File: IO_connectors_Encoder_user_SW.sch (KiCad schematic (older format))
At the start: 36 parts, among them IC1 TPD4E001DRLR, IC2 74AUP1G74DC.125, IC3 CD74HC4050PWR, SW1 TL1100CF160Q, SW2 PEC16-2215F-S0024, X1 DS1024-2*20R0, X2 DS1013-16SSIB1, X3 691322110005

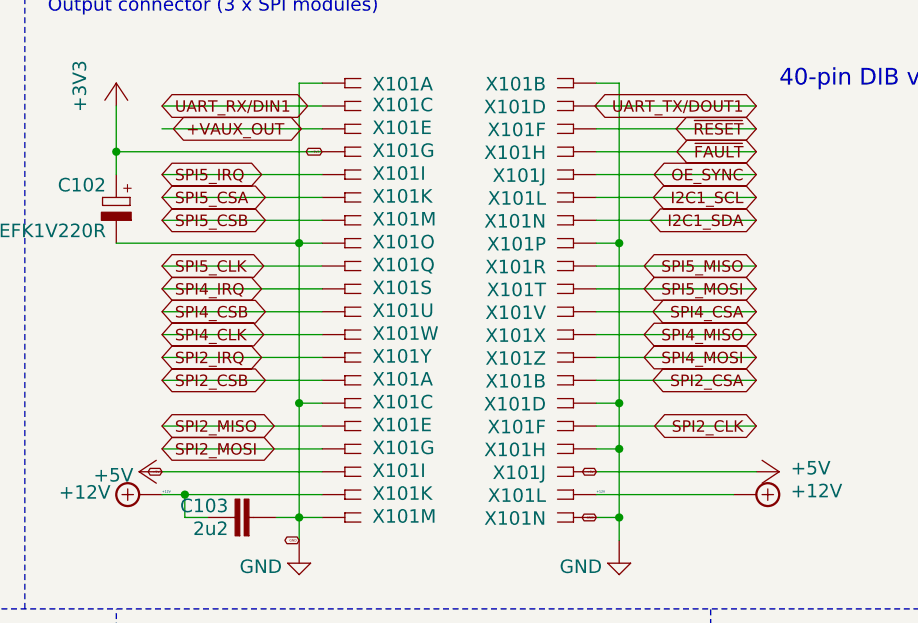
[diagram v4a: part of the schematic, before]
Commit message: Adding TO FROM FPGA lines
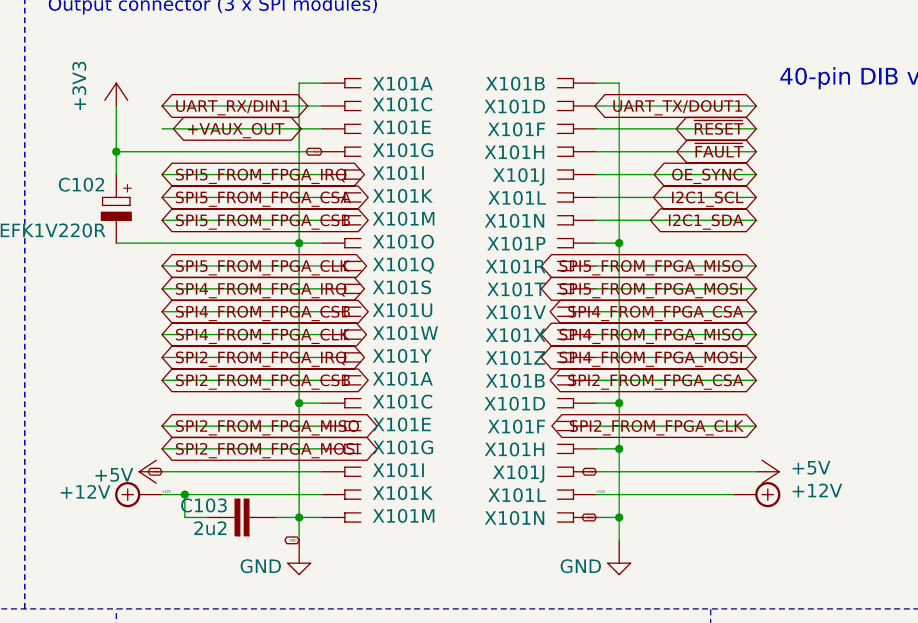
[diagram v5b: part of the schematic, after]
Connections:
- net SPI2_CLK renamed SPI2_FROM_FPGA_CLK
- net SPI2_CSA renamed SPI2_FROM_FPGA_CSA
- net SPI2_CSB renamed SPI2_FROM_FPGA_CSB
- net SPI2_IRQ renamed SPI2_FROM_FPGA_IRQ
- net SPI2_MISO renamed SPI2_FROM_FPGA_MISO
- net SPI2_MOSI renamed SPI2_FROM_FPGA_MOSI
- net SPI4_CLK renamed SPI4_FROM_FPGA_CLK
- net SPI4_CSA renamed SPI4_FROM_FPGA_CSA
- net SPI4_CSB renamed SPI4_FROM_FPGA_CSB
- net SPI4_IRQ renamed SPI4_FROM_FPGA_IRQ
- net SPI4_MISO renamed SPI4_FROM_FPGA_MISO
- net SPI4_MOSI renamed SPI4_FROM_FPGA_MOSI
- net SPI5_CLK renamed SPI5_FROM_FPGA_CLK
- net SPI5_CSA renamed SPI5_FROM_FPGA_CSA
- net SPI5_CSB renamed SPI5_FROM_FPGA_CSB
- net SPI5_IRQ renamed SPI5_FROM_FPGA_IRQ
- net SPI5_MISO renamed SPI5_FROM_FPGA_MISO
- net SPI5_MOSI renamed SPI5_FROM_FPGA_MOSI
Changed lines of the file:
@@
 	8600 2600 9300 2600
 Text GLabel 9300 2600 0    50   BiDi ~ 0
-SPI2_CLK
+SPI2_FROM_FPGA_CLK
 Wire Wire Line
 	7400 2600 6700 2600
 Text GLabel 6700 2600 2    50   BiDi ~ 0
-SPI2_MISO
+SPI2_FROM_FPGA_MISO
 Wire Wire Line
 	7400 2700 6700 2700
 Text GLabel 6700 2700 2    50   BiDi ~ 0
-SPI2_MOSI
+SPI2_FROM_FPGA_MOSI
 Wire Wire Line
 	8600 2400 9300 2400
 Text GLabel 9300 2400 0    50   BiDi ~ 0
-SPI2_CSA
+SPI2_FROM_FPGA_CSA
 Wire Wire Line
 	7400 2400 6700 2400
 Text GLabel 6700 2400 2    50   BiDi ~ 0
-SPI2_CSB
+SPI2_FROM_FPGA_CSB
 Wire Wire Line
 	7400 2300 6700 2300
 Text GLabel 6700 2300 2    50   BiDi ~ 0
-SPI2_IRQ
+SPI2_FROM_FPGA_IRQ
 Wire Wire Line
 	7400 1900 6700 1900
 Text GLabel 6700 1900 2    50   BiDi ~ 0
-SPI5_CLK
+SPI5_FROM_FPGA_CLK
 Wire Wire Line
 	8600 1900 9300 1900
 Text GLabel 9300 1900 0    50   BiDi ~ 0
-SPI5_MISO
+SPI5_FROM_FPGA_MISO
 Wire Wire Line
 	8600 2000 9300 2000
 Text GLabel 9300 2000 0    50   BiDi ~ 0
-SPI5_MOSI
+SPI5_FROM_FPGA_MOSI
 Wire Wire Line
 	7400 1600 6700 1600
 Text GLabel 6700 1600 2    50   BiDi ~ 0
-SPI5_CSA
+SPI5_FROM_FPGA_CSA
 Wire Wire Line
 	7400 1700 6700 1700
 Text GLabel 6700 1700 2    50   BiDi ~ 0
-SPI5_CSB
+SPI5_FROM_FPGA_CSB
 Wire Wire Line
 	7400 1500 6700 1500
 Text GLabel 6700 1500 2    50   BiDi ~ 0
-SPI5_IRQ
+SPI5_FROM_FPGA_IRQ
 Wire Wire Line
 	7400 2200 6700 2200
 Text GLabel 6700 2200 2    50   BiDi ~ 0
-SPI4_CLK
+SPI4_FROM_FPGA_CLK
 Wire Wire Line
 	8600 2200 9300 2200
 Text GLabel 9300 2200 0    50   BiDi ~ 0
-SPI4_MISO
+SPI4_FROM_FPGA_MISO
 Wire Wire Line
 	8600 2300 9300 2300
 Text GLabel 9300 2300 0    50   BiDi ~ 0
-SPI4_MOSI
+SPI4_FROM_FPGA_MOSI
 Wire Wire Line
 	8600 2100 9300 2100
 Text GLabel 9300 2100 0    50   BiDi ~ 0
-SPI4_CSA
+SPI4_FROM_FPGA_CSA
 Wire Wire Line
 	7400 2100 6700 2100
 Text GLabel 6700 2100 2    50   BiDi ~ 0
-SPI4_CSB
+SPI4_FROM_FPGA_CSB
 Wire Wire Line
 	7400 2000 6700 2000
 Text GLabel 6700 2000 2    50   BiDi ~ 0
-SPI4_IRQ
+SPI4_FROM_FPGA_IRQ
 Wire Wire Line
 	8600 1300 9300 1300

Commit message: Rewiering LCD OUT to bottom left
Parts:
- R1, R10, R11, R2, R3, R4, R5, R6, R7, R8, R9: footprint Resistor_SMD:R_0805_2012Metric -> Resistor_SMD:R_0603_1608Metric
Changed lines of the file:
@@
 F 0 "R102" H 8300 4759 59  0000 R BNN
 F 1 "10K" H 8300 4570 59  0000 R BNN
-F 2 "Resistor_SMD:R_0805_2012Metric" H 8200 4700 50  0001 C CNN
+F 2 "Resistor_SMD:R_0603_1608Metric" H 8200 4700 50  0001 C CNN
 F 3 "" H 8200 4700 50  0001 C CNN
 	1    8200 4700
@@
 F 0 "R101" V 7809 4450 59  0000 R TNN
 F 1 "4K7" V 7895 4450 59  0000 R TNN
-F 2 "Resistor_SMD:R_0805_2012Metric" H 7900 4500 50  0001 C CNN
+F 2 "Resistor_SMD:R_0603_1608Metric" H 7900 4500 50  0001 C CNN
 F 3 "" H 7900 4500 50  0001 C CNN
 	1    7900 4500
@@
 F 0 "R107" V 7609 4950 59  0000 R TNN
 F 1 "4K7" V 7695 4950 59  0000 R TNN
-F 2 "Resistor_SMD:R_0805_2012Metric" H 7700 5000 50  0001 C CNN
+F 2 "Resistor_SMD:R_0603_1608Metric" H 7700 5000 50  0001 C CNN
 F 3 "" H 7700 5000 50  0001 C CNN
 	1    7700 5000
@@
 F 0 "R111" H 8100 5459 59  0000 R BNN
 F 1 "10K" H 8100 5270 59  0000 R BNN
-F 2 "Resistor_SMD:R_0805_2012Metric" H 8000 5400 50  0001 C CNN
+F 2 "Resistor_SMD:R_0603_1608Metric" H 8000 5400 50  0001 C CNN
 F 3 "" H 8000 5400 50  0001 C CNN
 	1    8000 5400
@@
 F 0 "R105" H 3150 4741 59  0000 L TNN
 F 1 "4K7" H 3125 4930 59  0000 L TNN
-F 2 "Resistor_SMD:R_0805_2012Metric" H 3200 4800 50  0001 C CNN
+F 2 "Resistor_SMD:R_0603_1608Metric" H 3200 4800 50  0001 C CNN
 F 3 "" H 3200 4800 50  0001 C CNN
 	1    3200 4800
@@
 F 0 "R104" H 2650 4741 59  0000 L TNN
 F 1 "4K7" H 2600 4930 59  0000 L TNN
-F 2 "Resistor_SMD:R_0805_2012Metric" H 2700 4800 50  0001 C CNN
+F 2 "Resistor_SMD:R_0603_1608Metric" H 2700 4800 50  0001 C CNN
 F 3 "" H 2700 4800 50  0001 C CNN
 	1    2700 4800
@@
 F 0 "R109" H 3150 5141 59  0000 L TNN
 F 1 "4K7" H 3125 5330 59  0000 L TNN
-F 2 "Resistor_SMD:R_0805_2012Metric" H 3200 5200 50  0001 C CNN
+F 2 "Resistor_SMD:R_0603_1608Metric" H 3200 5200 50  0001 C CNN
 F 3 "" H 3200 5200 50  0001 C CNN
 	1    3200 5200
@@
 F 0 "R108" H 2650 5141 59  0000 L TNN
 F 1 "4K7" H 2625 5330 59  0000 L TNN
-F 2 "Resistor_SMD:R_0805_2012Metric" H 2700 5200 50  0001 C CNN
+F 2 "Resistor_SMD:R_0603_1608Metric" H 2700 5200 50  0001 C CNN
 F 3 "" H 2700 5200 50  0001 C CNN
 	1    2700 5200
@@
 F 0 "R106" H 4825 4684 59  0000 L BNN
 F 1 "1K" H 4850 4930 59  0000 L TNN
-F 2 "Resistor_SMD:R_0805_2012Metric" H 4900 4800 50  0001 C CNN
+F 2 "Resistor_SMD:R_0603_1608Metric" H 4900 4800 50  0001 C CNN
 F 3 "" H 4900 4800 50  0001 C CNN
 	1    4900 4800
@@
 F 0 "R110" H 4825 5084 59  0000 L BNN
 F 1 "1K" H 4850 5330 59  0000 L TNN
-F 2 "Resistor_SMD:R_0805_2012Metric" H 4900 5200 50  0001 C CNN
+F 2 "Resistor_SMD:R_0603_1608Metric" H 4900 5200 50  0001 C CNN
 F 3 "" H 4900 5200 50  0001 C CNN
 	1    4900 5200
@@
 F 0 "R103" H 9675 4641 59  0000 R TNN
 F 1 "10K" H 9675 4830 59  0000 R TNN
-F 2 "Resistor_SMD:R_0805_2012Metric" H 9600 4700 50  0001 C CNN
+F 2 "Resistor_SMD:R_0603_1608Metric" H 9600 4700 50  0001 C CNN
 F 3 "" H 9600 4700 50  0001 C CNN
 	1    9600 4700

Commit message: More schematics cleanup
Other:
- moved on the sheet: C102

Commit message: Almost ready for routing
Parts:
- removed JP2: JP2-NOCUT, EEZ DIB MCU r3B4:JP2-NOCUT, symbol IO_connectors_Encoder_user_SW-rescue:JP2-NOCUT-EEZ_DIB_MCU_r3B4-eagle-import
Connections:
- net I2C1_SDA: now also X2.14 (1)
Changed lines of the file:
@@
 	1900 2200 2100 2200
-Wire Wire Line
-	3300 2200 3500 2200
 Wire Wire Line
 	3700 3900 2400 3900
@@
 F 3 "" H 1800 2200 50  0001 C CNN
 	1    1800 2200
-	1    0    0    -1
-$EndComp
-$Comp
-L IO_connectors_Encoder_user_SW-rescue:JP2-NOCUT-EEZ_DIB_MCU_r3B4-eagle-import JP2
-U 1 1 FA93C76E
-P 3500 2200
-AR Path="/4804D7FCFA93C76E" Ref="JP2"  Part="1"
-AR Path="/5F88C8A0/4804D7FCFA93C76E" Ref="JP2"  Part="1"
-AR Path="/5F8FDB74/FA93C76E" Ref="JP102"  Part="1"
-F 0 "JP102" H 3475 2225 59  0000 L BNN
-F 1 "JP2-NOCUT" H 3500 2200 50  0001 C CNN
-F 2 "EEZ DIB MCU r3B4:JP2-NOCUT" H 3500 2200 50  0001 C CNN
-F 3 "" H 3500 2200 50  0001 C CNN
-	1    3500 2200
 	1    0    0    -1
 $EndComp
@@
 	3300 2100 3700 2100
 Wire Wire Line
-	3700 2200 3600 2200
-Wire Wire Line
 	3700 1600 3300 1600
 Wire Wire Line
@@
 Wire Wire Line
 	8600 2400 8800 2400
+Wire Wire Line
+	3300 2200 3700 2200
 $EndSCHEMATC
